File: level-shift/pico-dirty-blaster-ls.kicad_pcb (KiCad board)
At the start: 2 copper layers, 15.2 x 50.8 mm, 14 parts, among them J1 Conn_01x20, J2 Conn_02x05_Odd_Even, J3 Conn_01x04, J4 Conn_02x05_Odd_Even, SW1 SW_Push, U1 TXB0104PW, U6 TS5A63157DBV

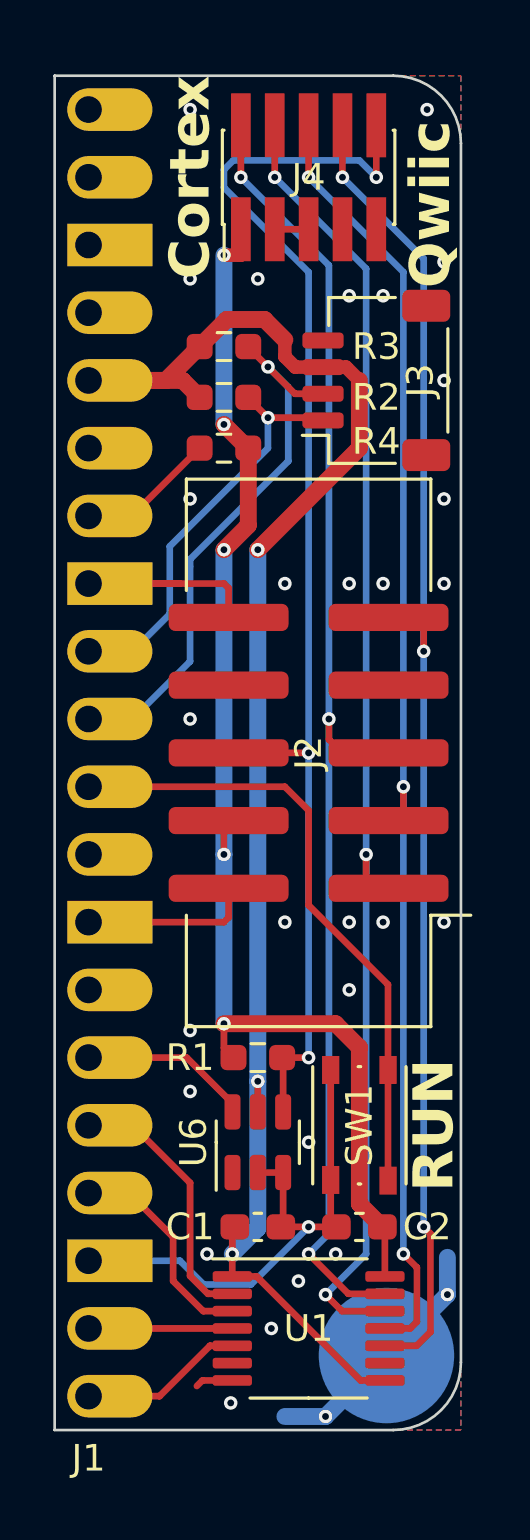
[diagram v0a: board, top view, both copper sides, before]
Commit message: changed reset level shift to pass FET
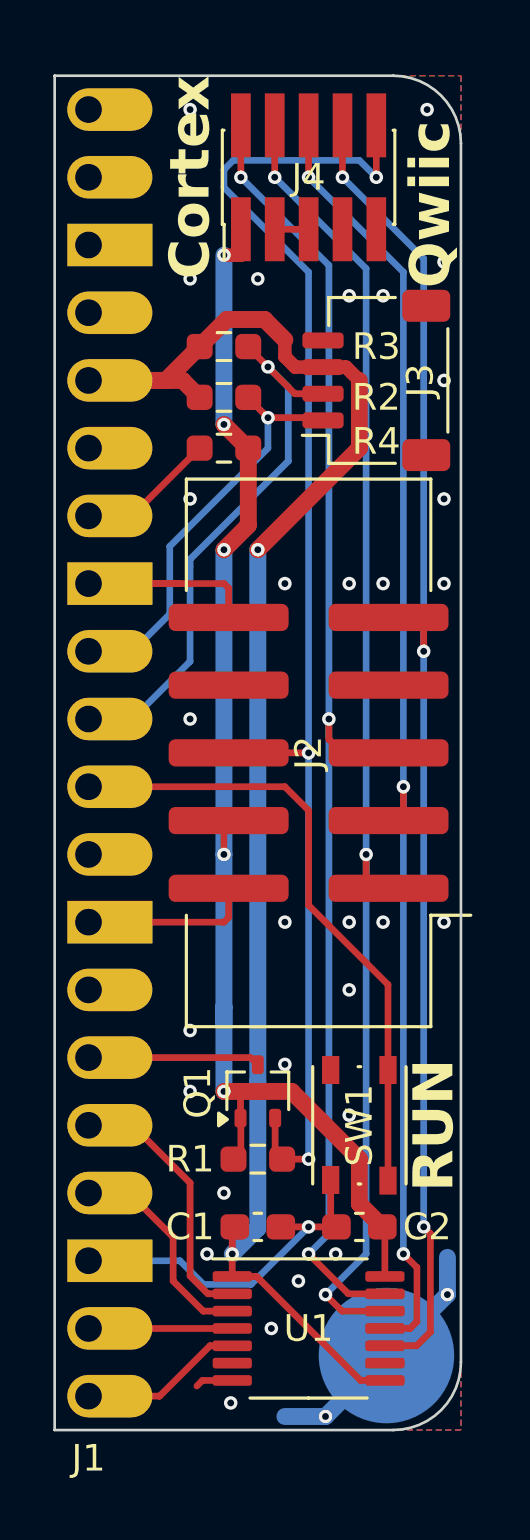
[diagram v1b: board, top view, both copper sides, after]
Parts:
- removed U6: TS5A63157DBV, Package_TO_SOT_SMD:SOT-23-6
- added Q1: RU1J002YNTCL, Package_TO_SOT_SMD:SOT-323_SC-70, F.Cu at (147.3, 114.3)
- moved R1 3.81 mm to (147.3, 116.8)
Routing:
- net GND: track 47.4 -> 40.3 mm, vias 31 -> 33
- net /VRST: track 48.7 -> 52.1 mm
- net +3.3V: track 62.0 -> 60.8 mm, vias 3 -> 2
- net VCC: track 48.4 -> 49.3 mm

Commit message: connected vcc on SM, 0402 R on LS
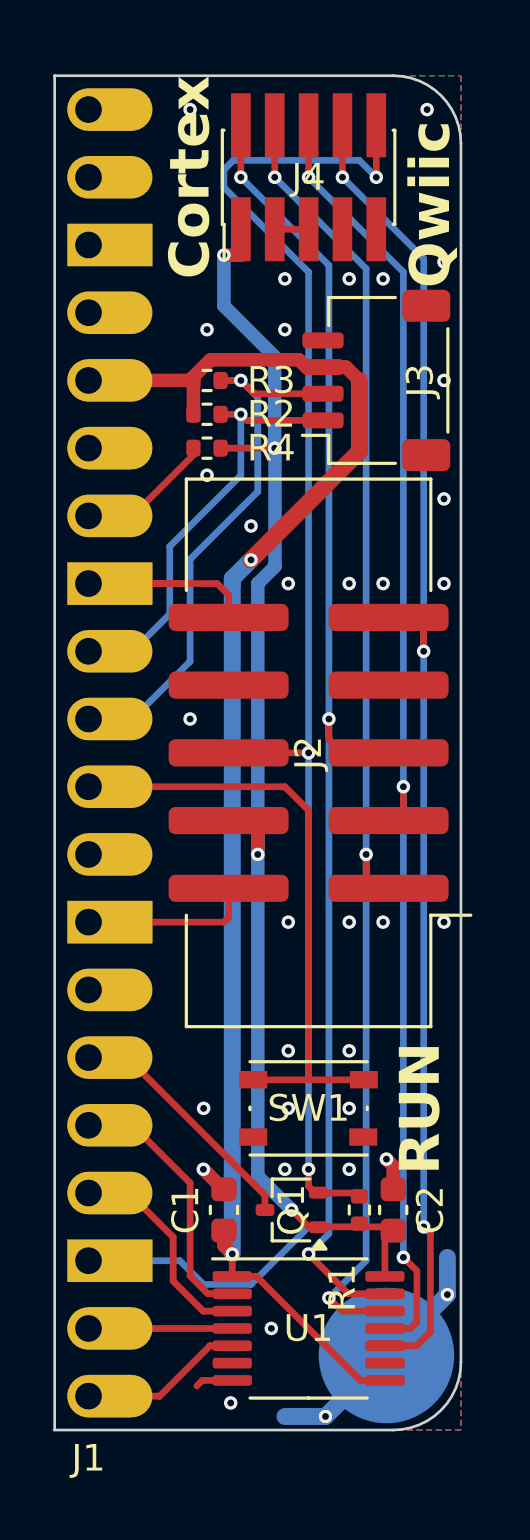
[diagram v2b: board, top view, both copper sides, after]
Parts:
- C1, C2: footprint Capacitor_SMD:C_0603_1608Metric_Pad1.08x0.95mm_HandSolder -> Capacitor_SMD:C_0603_1608Metric
- R1, R2, R3, R4: footprint Resistor_SMD:R_0603_1608Metric_Pad0.98x0.95mm_HandSolder -> Resistor_SMD:R_0402_1005Metric
- moved Q1 4.62 mm to (148.6, 118.7), turned to 180 degrees
- moved R1 4.26 mm to (151.1, 118.7), turned to 90 degrees
- moved SW1 2.01 mm to (149.2, 114.9), turned to 0 degrees
- moved R3 1.42 mm to (145.4, 87.6)
- moved C2 1.42 mm to (152.4, 118.7), turned to 90 degrees
- moved C1 1.42 mm to (146.1, 118.7), turned to 90 degrees
- moved R2 0.90 mm to (145.4, 88.9)
- moved R4 0.64 mm to (145.4, 90.2)
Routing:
- net +3.3V: track 60.8 -> 56.1 mm
- net /RST: track 6.46 -> 9.31 mm
- net GND: track 40.3 -> 38.5 mm, vias 33 -> 34
- net /RUN: track 23.7 -> 22.9 mm
- net /SDA: track 21.1 -> 20.6 mm
- net VCC: track 49.3 -> 49.5 mm, vias 5 -> 4

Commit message: fixed part number on level shifter
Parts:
- U1: value TXB0104PW -> TXU0304PW
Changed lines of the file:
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@@
         (effects (font (size 1 1) (thickness 0.15)))
     )
-    (fp_text value "TXB0104PW" (at 0 3.45) (layer "F.Fab")
+    (fp_text value "TXU0304PW" (at 0 3.45) (layer "F.Fab")
         (effects (font (size 1 1) (thickness 0.15)))
     )
